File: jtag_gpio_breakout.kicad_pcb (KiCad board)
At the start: 2 copper layers, 40.6 x 41.9 mm, 4 parts, among them J1 Conn_02x04_Odd_Even, J6 Conn_02x25_Odd_Even, J7 Conn_01x08, J8 Conn_02x04_Odd_Even

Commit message: jason - fixed some island issues
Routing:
- net AGND: track 55.9 -> 31.1 mm, vias 13 -> 9
- net AVDD: track 57.5 -> 52.1 mm, vias 14 -> 11
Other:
- board text removed: "P0.2"

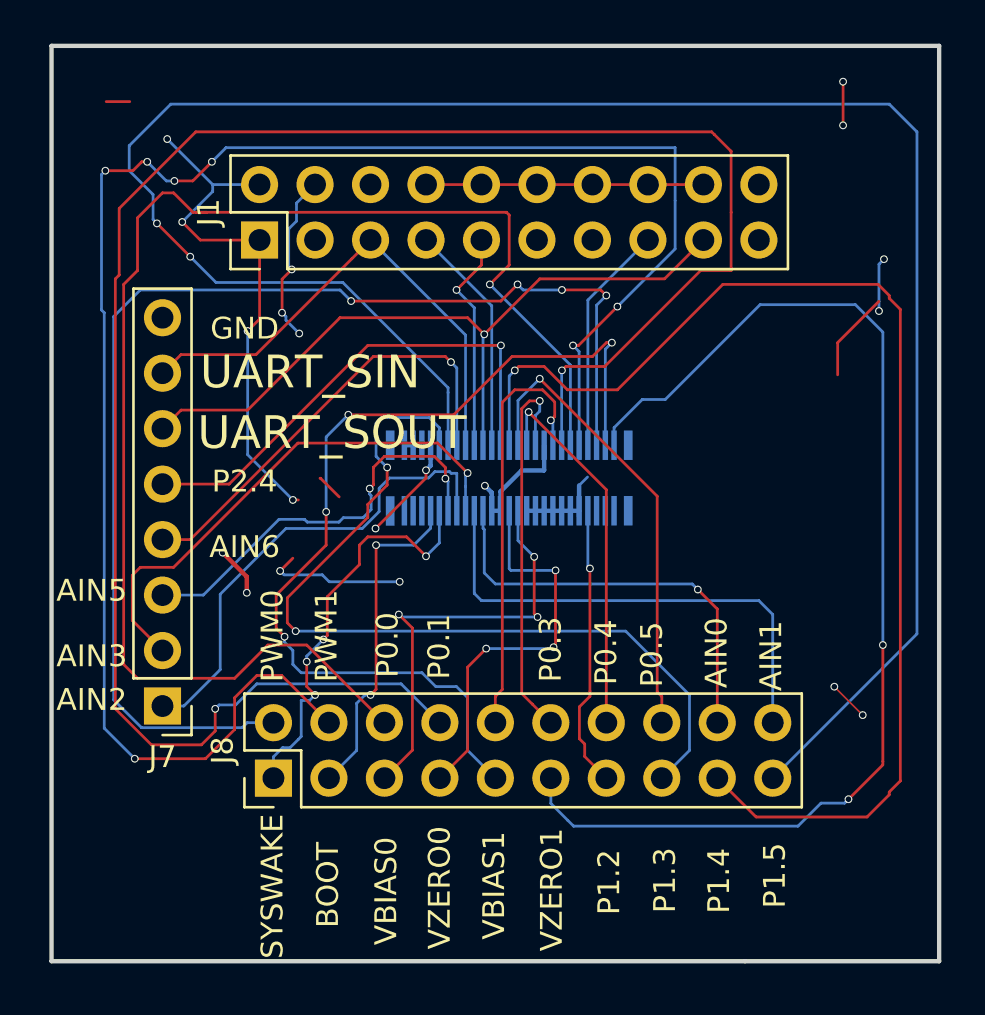
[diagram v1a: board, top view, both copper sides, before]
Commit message: updating repo to reflect fabricated project
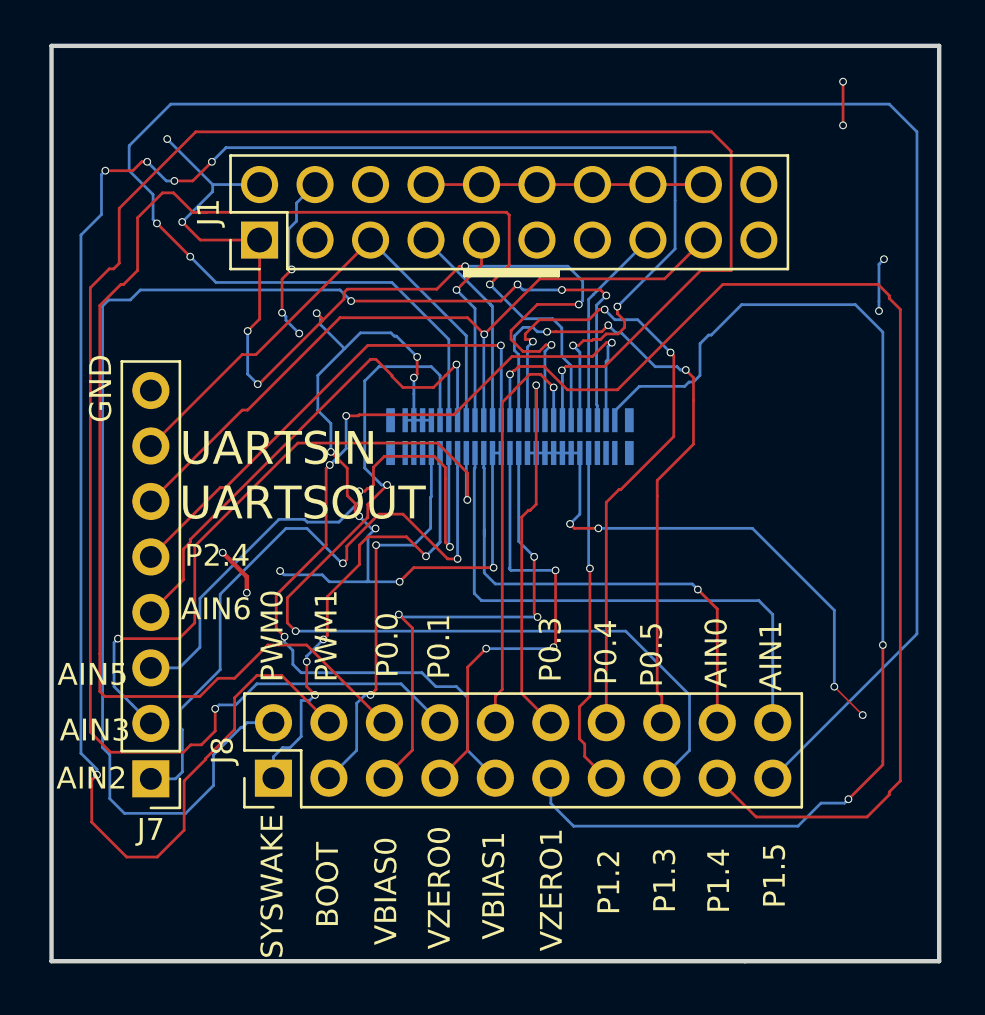
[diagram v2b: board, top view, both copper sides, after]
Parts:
- moved J7 3.38 mm to (141.7, 132.6)
- moved J6 1.85 mm to (158.2, 116.9)
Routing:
- net AVDD: track 52.1 -> 88.6 mm, vias 11 -> 18
- net AGND: track 31.1 -> 49.8 mm, vias 9 -> 11
- net /P0.4_I2C_SCL: track 17.3 -> 30.6 mm, vias 1 -> 3
- net /PWM1: track 82.9 -> 92.1 mm
- net /AIN5: track 19.1 -> 27.9 mm
- net /P0.5_I2C_SDA: track 21.5 -> 30.1 mm, vias 1 -> 3
- net /AIN2: track 22.3 -> 30.3 mm, vias 0 -> 2
- net /PWM0: track 56.3 -> 63.0 mm
- net /AIN3: track 24.2 -> 30.4 mm, vias 1 -> 2
- net /P1.3_SPI1_MOSI: track 39.4 -> 43.7 mm
- net /AIN0: track 19.4 -> 22.3 mm
- net /P1.0: track 18.9 -> 21.8 mm
- net /P0.0_SPI0_CLK: track 65.9 -> 68.5 mm
- net /P1.1: track 15.3 -> 18.0 mm
- net /AIN1: track 22.8 -> 25.5 mm
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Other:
- board text added: "UARTSIN"
- board text added: "UARTSOUT"
- board text removed: "UART_SIN"
- board text removed: "UART_SOUT"
